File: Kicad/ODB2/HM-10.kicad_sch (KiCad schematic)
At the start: 8 parts, among them J5 Conn_01x02_Pin

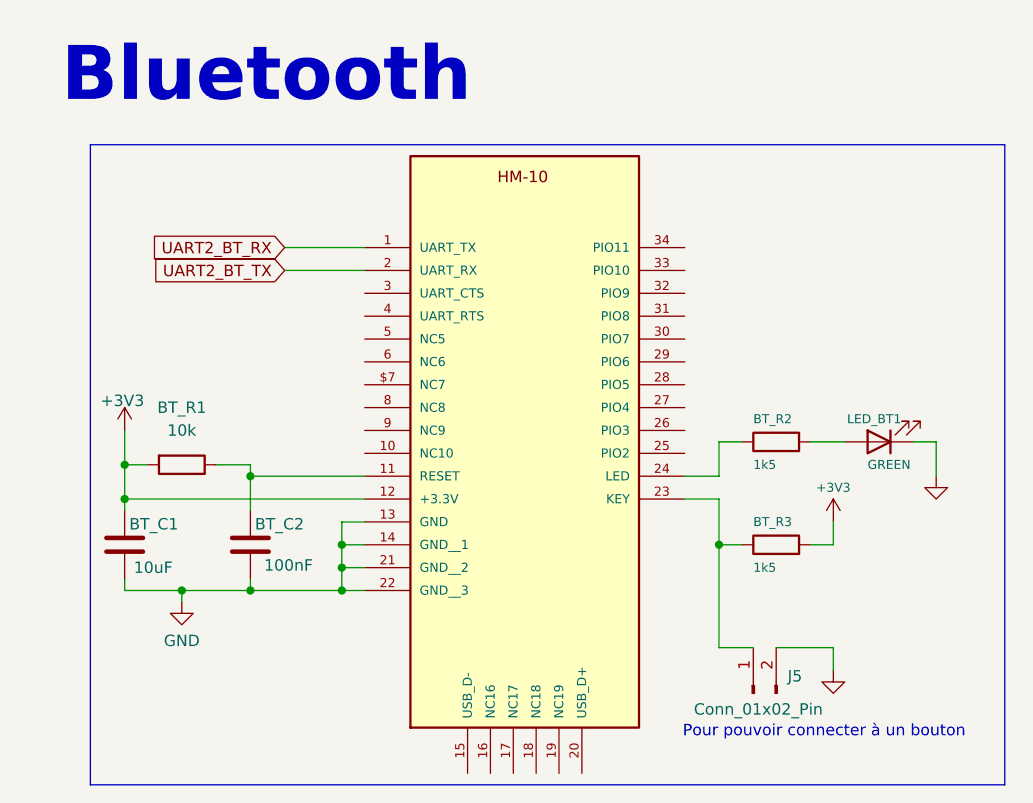
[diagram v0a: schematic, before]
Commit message: fix pinout
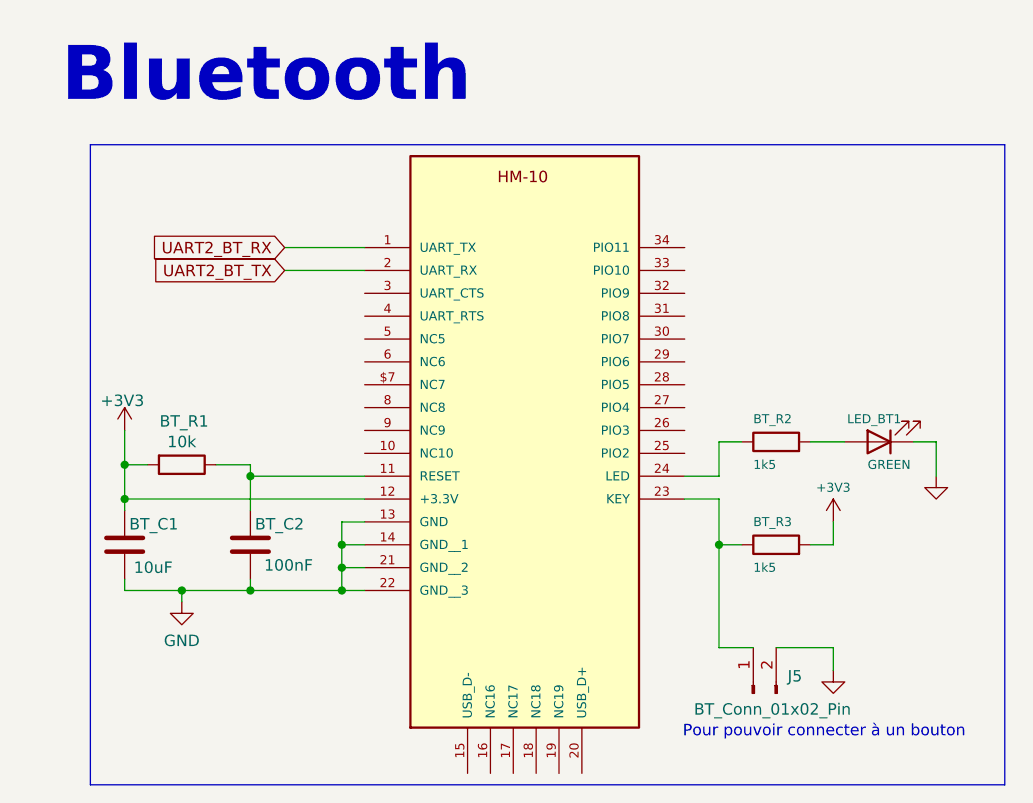
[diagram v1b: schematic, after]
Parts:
- J5: value Conn_01x02_Pin -> BT_Conn_01x02_Pin
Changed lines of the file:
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@@
 		(on_board yes)
 		(dnp no)
-		(fields_autoplaced yes)
 		(property "Reference" "BT_R1"
-			(at 25.4 54.61 90)
+			(at 25.654 56.134 90)
 			(effects
 				(font
@@
 		)
 		(property "Value" "10k"
-			(at 25.4 57.15 90)
+			(at 25.4 58.42 90)
 			(effects
 				(font
@@
 			)
 		)
-		(property "Value" "Conn_01x02_Pin"
+		(property "Value" "BT_Conn_01x02_Pin"
 			(at 82.296 88.138 90)
 			(effects

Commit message: Revert "fix pinout"
This reverts commit f7fb1bb1343b18ec7defcf1dc44a3e70818eed55.
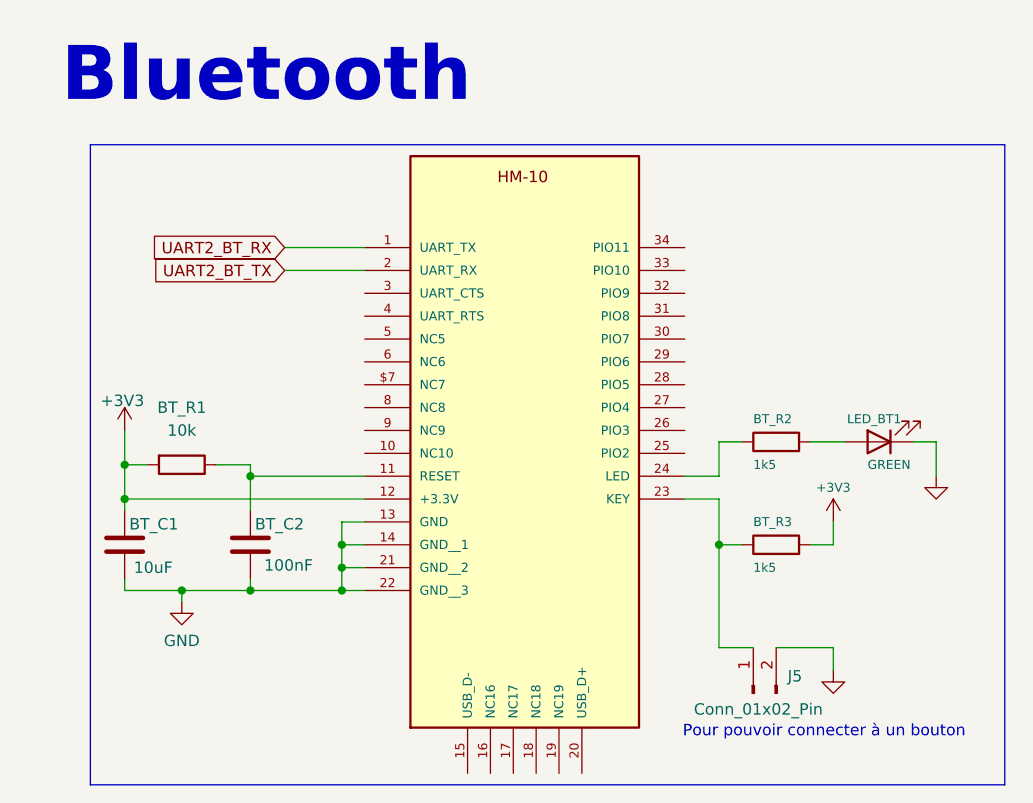
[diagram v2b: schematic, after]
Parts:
- J5: value BT_Conn_01x02_Pin -> Conn_01x02_Pin
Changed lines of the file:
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@@
 		(on_board yes)
 		(dnp no)
+		(fields_autoplaced yes)
 		(property "Reference" "BT_R1"
-			(at 25.654 56.134 90)
+			(at 25.4 54.61 90)
 			(effects
 				(font
@@
 		)
 		(property "Value" "10k"
-			(at 25.4 58.42 90)
+			(at 25.4 57.15 90)
 			(effects
 				(font
@@
 			)
 		)
-		(property "Value" "BT_Conn_01x02_Pin"
+		(property "Value" "Conn_01x02_Pin"
 			(at 82.296 88.138 90)
 			(effects
